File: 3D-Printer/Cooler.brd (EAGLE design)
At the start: 100 x 75 mm, 39 parts, among them IC1 L293D, IC2 REG1117

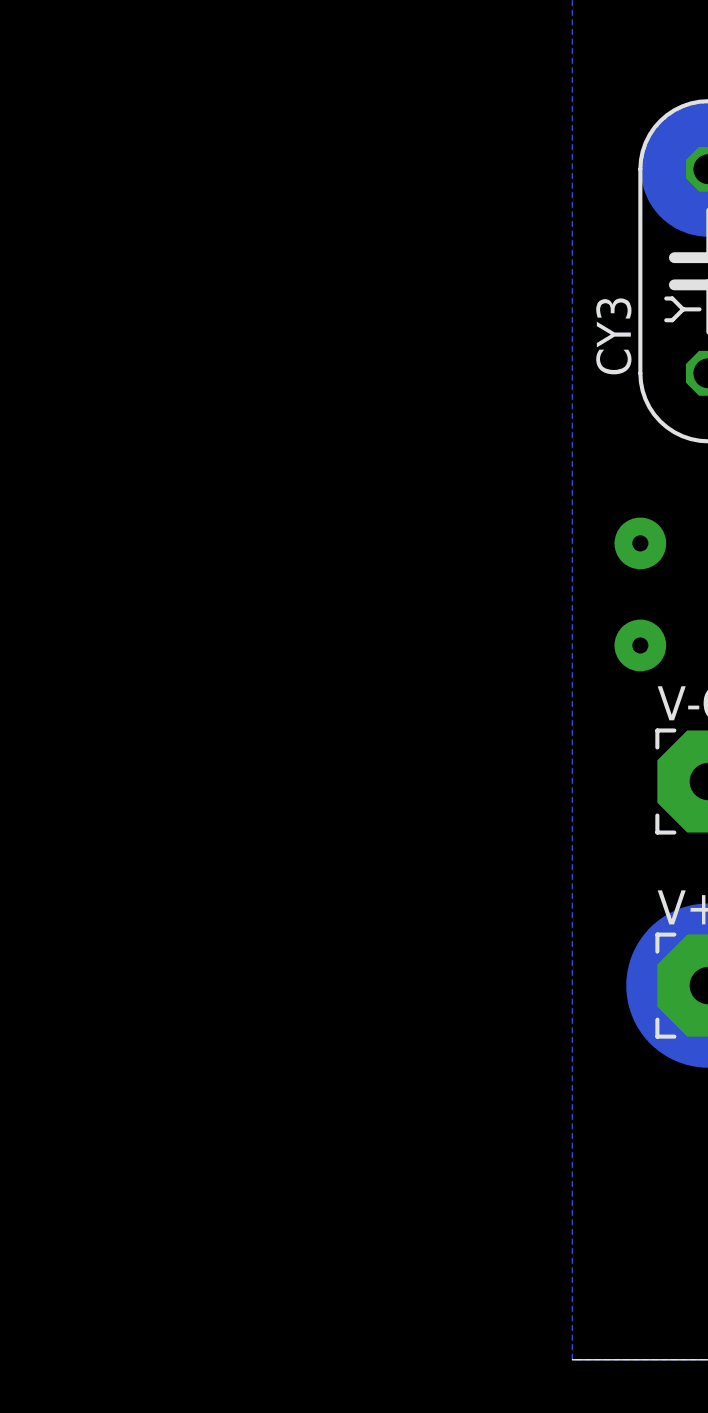
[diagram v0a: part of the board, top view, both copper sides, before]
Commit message: correct meters
meters and serial needed reversed.
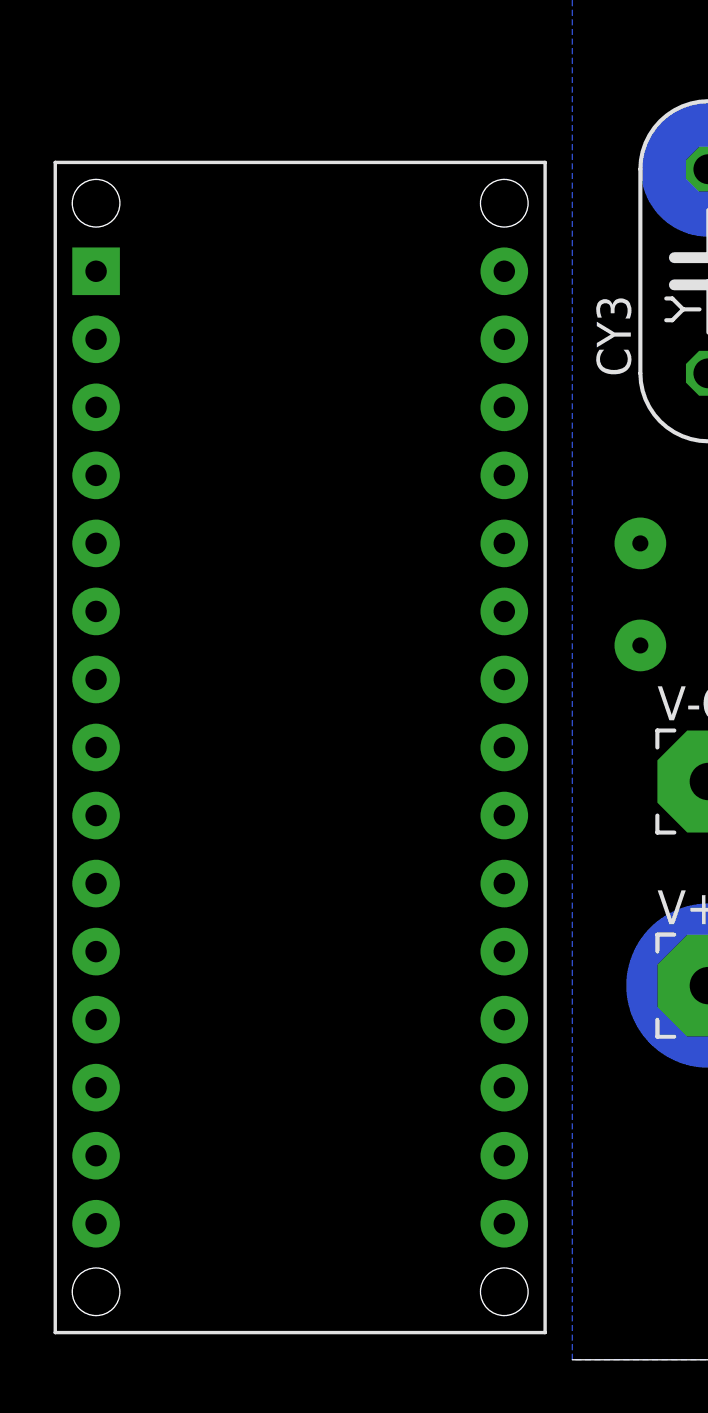
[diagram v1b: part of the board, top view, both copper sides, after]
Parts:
- added U$2: ARDUINONANO, CRE-Lib1:PDIP-32
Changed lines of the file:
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@@
 <grid distance="2.54" unitdist="mm" unit="mm" style="lines" multiple="1" display="yes" altdistance="1.27" altunitdist="mm" altunit="mm"/>
 <layers>
-<layer number="1" name="Top" color="4" fill="1" visible="yes" active="yes"/>
+<layer number="1" name="Top" color="4" fill="1" visible="no" active="yes"/>
 <layer number="2" name="Route2" color="1" fill="3" visible="no" active="yes"/>
 <layer number="3" name="Route3" color="4" fill="3" visible="no" active="yes"/>
@@
 <layer number="17" name="Pads" color="2" fill="1" visible="yes" active="yes"/>
 <layer number="18" name="Vias" color="2" fill="1" visible="yes" active="yes"/>
-<layer number="19" name="Unrouted" color="6" fill="1" visible="yes" active="yes"/>
-<layer number="20" name="Dimension" color="15" fill="1" visible="yes" active="yes"/>
-<layer number="21" name="tPlace" color="7" fill="1" visible="yes" active="yes"/>
-<layer number="22" name="bPlace" color="7" fill="1" visible="yes" active="yes"/>
-<layer number="23" name="tOrigins" color="15" fill="1" visible="yes" active="yes"/>
-<layer number="24" name="bOrigins" color="15" fill="1" visible="yes" active="yes"/>
-<layer number="25" name="tNames" color="7" fill="1" visible="yes" active="yes"/>
-<layer number="26" name="bNames" color="7" fill="1" visible="yes" active="yes"/>
-<layer number="27" name="tValues" color="7" fill="1" visible="yes" active="yes"/>
-<layer number="28" name="bValues" color="7" fill="1" visible="yes" active="yes"/>
+<layer number="19" name="Unrouted" color="6" fill="1" visible="no" active="yes"/>
+<layer number="20" name="Dimension" color="15" fill="1" visible="no" active="yes"/>
+<layer number="21" name="tPlace" color="7" fill="1" visible="no" active="yes"/>
+<layer number="22" name="bPlace" color="7" fill="1" visible="no" active="yes"/>
+<layer number="23" name="tOrigins" color="15" fill="1" visible="no" active="yes"/>
+<layer number="24" name="bOrigins" color="15" fill="1" visible="no" active="yes"/>
+<layer number="25" name="tNames" color="7" fill="1" visible="no" active="yes"/>
+<layer number="26" name="bNames" color="7" fill="1" visible="no" active="yes"/>
+<layer number="27" name="tValues" color="7" fill="1" visible="no" active="yes"/>
+<layer number="28" name="bValues" color="7" fill="1" visible="no" active="yes"/>
 <layer number="29" name="tStop" color="7" fill="3" visible="no" active="yes"/>
 <layer number="30" name="bStop" color="7" fill="6" visible="no" active="yes"/>
@@
 <layer number="37" name="tTest" color="7" fill="1" visible="no" active="yes"/>
 <layer number="38" name="bTest" color="7" fill="1" visible="no" active="yes"/>
-<layer number="39" name="tKeepout" color="4" fill="11" visible="yes" active="yes"/>
-<layer number="40" name="bKeepout" color="1" fill="11" visible="yes" active="yes"/>
-<layer number="41" name="tRestrict" color="4" fill="10" visible="yes" active="yes"/>
-<layer number="42" name="bRestrict" color="1" fill="10" visible="yes" active="yes"/>
-<layer number="43" name="vRestrict" color="2" fill="10" visible="yes" active="yes"/>
+<layer number="39" name="tKeepout" color="4" fill="11" visible="no" active="yes"/>
+<layer number="40" name="bKeepout" color="1" fill="11" visible="no" active="yes"/>
+<layer number="41" name="tRestrict" color="4" fill="10" visible="no" active="yes"/>
+<layer number="42" name="bRestrict" color="1" fill="10" visible="no" active="yes"/>
+<layer number="43" name="vRestrict" color="2" fill="10" visible="no" active="yes"/>
 <layer number="44" name="Drills" color="7" fill="1" visible="no" active="yes"/>
-<layer number="45" name="Holes" color="7" fill="1" visible="yes" active="yes"/>
+<layer number="45" name="Holes" color="7" fill="1" visible="no" active="yes"/>
 <layer number="46" name="Milling" color="3" fill="1" visible="no" active="yes"/>
 <layer number="47" name="Measures" color="7" fill="1" visible="no" active="yes"/>
-<layer number="48" name="Document" color="7" fill="1" visible="yes" active="yes"/>
-<layer number="49" name="Reference" color="7" fill="1" visible="yes" active="yes"/>
+<layer number="48" name="Document" color="7" fill="1" visible="no" active="yes"/>
+<layer number="49" name="Reference" color="7" fill="1" visible="no" active="yes"/>
 <layer number="50" name="dxf" color="7" fill="1" visible="no" active="yes"/>
-<layer number="51" name="tDocu" color="7" fill="1" visible="yes" active="yes"/>
-<layer number="52" name="bDocu" color="7" fill="1" visible="yes" active="yes"/>
+<layer number="51" name="tDocu" color="7" fill="1" visible="no" active="yes"/>
+<layer number="52" name="bDocu" color="7" fill="1" visible="no" active="yes"/>
 <layer number="53" name="tGND_GNDA" color="7" fill="9" visible="no" active="no"/>
 <layer number="54" name="bGND_GNDA" color="1" fill="9" visible="no" active="no"/>
@@
 <layer number="127" name="_tValues" color="7" fill="1" visible="no" active="yes"/>
 <layer number="128" name="_bValues" color="7" fill="1" visible="no" active="yes"/>
-<layer number="129" name="Mask" color="7" fill="1" visible="yes" active="yes"/>
+<layer number="129" name="Mask" color="7" fill="1" visible="no" active="yes"/>
 <layer number="131" name="tAdjust" color="7" fill="1" visible="no" active="yes"/>
 <layer number="132" name="bAdjust" color="7" fill="1" visible="no" active="yes"/>
@@
 <layer number="223" name="223bmp" color="24" fill="1" visible="no" active="no"/>
 <layer number="224" name="224bmp" color="25" fill="1" visible="no" active="no"/>
-<layer number="225" name="225bmp" color="7" fill="1" visible="yes" active="yes"/>
-<layer number="226" name="226bmp" color="7" fill="1" visible="yes" active="yes"/>
-<layer number="227" name="227bmp" color="7" fill="1" visible="yes" active="yes"/>
-<layer number="228" name="228bmp" color="7" fill="1" visible="yes" active="yes"/>
-<layer number="229" name="229bmp" color="7" fill="1" visible="yes" active="yes"/>
-<layer number="230" name="230bmp" color="7" fill="1" visible="yes" active="yes"/>
+<layer number="225" name="225bmp" color="7" fill="1" visible="no" active="yes"/>
+<layer number="226" name="226bmp" color="7" fill="1" visible="no" active="yes"/>
+<layer number="227" name="227bmp" color="7" fill="1" visible="no" active="yes"/>
+<layer number="228" name="228bmp" color="7" fill="1" visible="no" active="yes"/>
+<layer number="229" name="229bmp" color="7" fill="1" visible="no" active="yes"/>
+<layer number="230" name="230bmp" color="7" fill="1" visible="no" active="yes"/>
 <layer number="231" name="Eagle3D_PG1" color="7" fill="1" visible="no" active="no"/>
 <layer number="232" name="Eagle3D_PG2" color="7" fill="1" visible="no" active="no"/>
@@
 <layer number="251" name="SMDround" color="7" fill="1" visible="no" active="no"/>
 <layer number="254" name="cooling" color="7" fill="1" visible="no" active="yes"/>
-<layer number="255" name="routoute" color="7" fill="1" visible="yes" active="yes"/>
+<layer number="255" name="routoute" color="7" fill="1" visible="no" active="yes"/>
 </layers>
 <board>
@@
 <element name="PAD3" library="wirepad" package="3,81/1,4" value="WIREPAD3,81/1,4" x="59.69" y="52.07"/>
 <element name="CY5" library="resistor" package="YC7B5" value="" x="38.1" y="10.16" rot="R90"/>
+<element name="U$2" library="CRE-Lib1" package="PDIP-32" value="ARDUINONANO" x="-17.78" y="43.18"/>
 </elements>
 <signals>

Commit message: Added bounce capacitor
Corrected bounce on switch
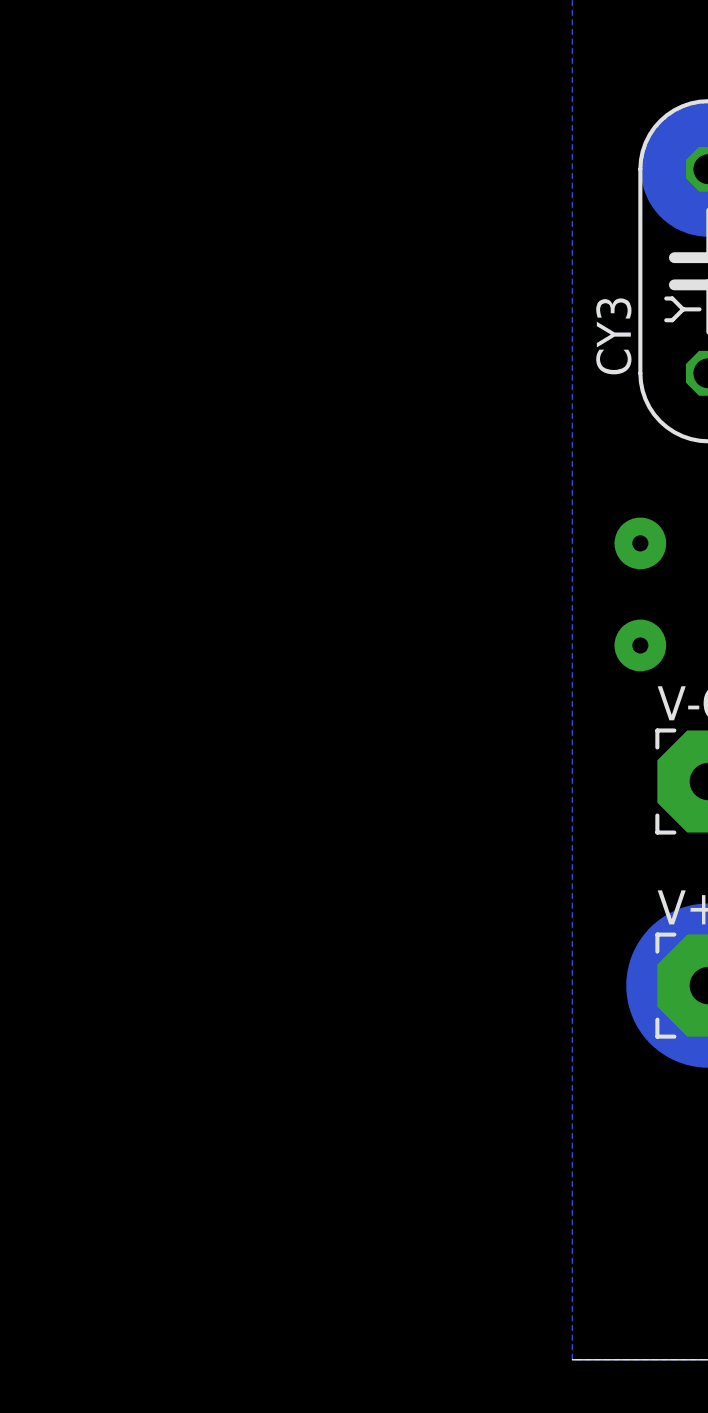
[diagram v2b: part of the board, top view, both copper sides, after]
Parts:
- removed U$2: ARDUINONANO, CRE-Lib1:PDIP-32
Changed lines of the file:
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@@
 <layer number="17" name="Pads" color="2" fill="1" visible="yes" active="yes"/>
 <layer number="18" name="Vias" color="2" fill="1" visible="yes" active="yes"/>
-<layer number="19" name="Unrouted" color="6" fill="1" visible="no" active="yes"/>
-<layer number="20" name="Dimension" color="15" fill="1" visible="no" active="yes"/>
-<layer number="21" name="tPlace" color="7" fill="1" visible="no" active="yes"/>
-<layer number="22" name="bPlace" color="7" fill="1" visible="no" active="yes"/>
-<layer number="23" name="tOrigins" color="15" fill="1" visible="no" active="yes"/>
-<layer number="24" name="bOrigins" color="15" fill="1" visible="no" active="yes"/>
-<layer number="25" name="tNames" color="7" fill="1" visible="no" active="yes"/>
-<layer number="26" name="bNames" color="7" fill="1" visible="no" active="yes"/>
-<layer number="27" name="tValues" color="7" fill="1" visible="no" active="yes"/>
-<layer number="28" name="bValues" color="7" fill="1" visible="no" active="yes"/>
+<layer number="19" name="Unrouted" color="6" fill="1" visible="yes" active="yes"/>
+<layer number="20" name="Dimension" color="15" fill="1" visible="yes" active="yes"/>
+<layer number="21" name="tPlace" color="7" fill="1" visible="yes" active="yes"/>
+<layer number="22" name="bPlace" color="7" fill="1" visible="yes" active="yes"/>
+<layer number="23" name="tOrigins" color="15" fill="1" visible="yes" active="yes"/>
+<layer number="24" name="bOrigins" color="15" fill="1" visible="yes" active="yes"/>
+<layer number="25" name="tNames" color="7" fill="1" visible="yes" active="yes"/>
+<layer number="26" name="bNames" color="7" fill="1" visible="yes" active="yes"/>
+<layer number="27" name="tValues" color="7" fill="1" visible="yes" active="yes"/>
+<layer number="28" name="bValues" color="7" fill="1" visible="yes" active="yes"/>
 <layer number="29" name="tStop" color="7" fill="3" visible="no" active="yes"/>
 <layer number="30" name="bStop" color="7" fill="6" visible="no" active="yes"/>
@@
 <element name="PAD3" library="wirepad" package="3,81/1,4" value="WIREPAD3,81/1,4" x="59.69" y="52.07"/>
 <element name="CY5" library="resistor" package="YC7B5" value="" x="38.1" y="10.16" rot="R90"/>
-<element name="U$2" library="CRE-Lib1" package="PDIP-32" value="ARDUINONANO" x="-17.78" y="43.18"/>
 </elements>
 <signals>
